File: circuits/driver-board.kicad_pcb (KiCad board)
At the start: 4 copper layers, 40 x 47 mm, 72 parts, among them J1 Conn_01x18_Female, J2 USB4120-03-C_REVA, J3 Motor_Conn_01x04, J4 Screw_Terminals, J5 Conn_01x06_Female, Q1 SS8050-G, Q2 SS8050-G, SW1 RST_SW_Push, U1 CP2102N-A01-GQFN24, U2 BA33DD0T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

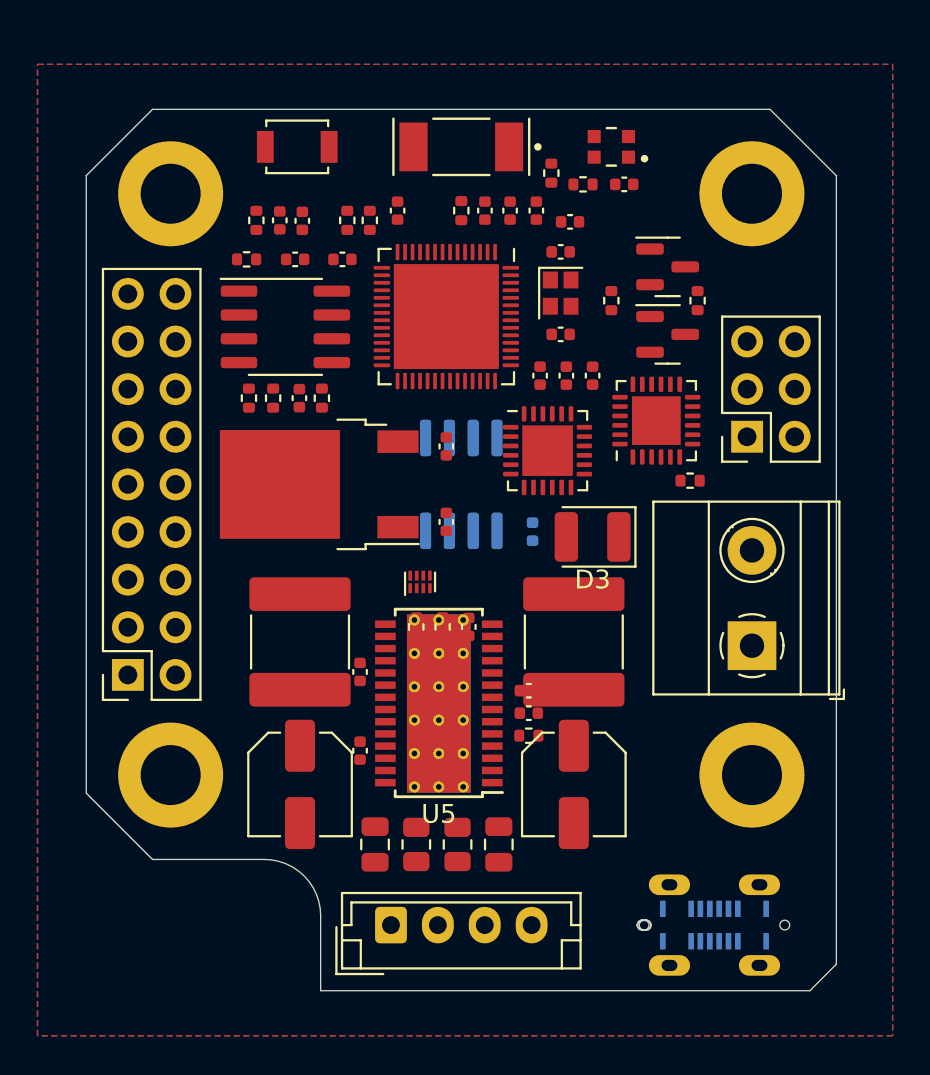
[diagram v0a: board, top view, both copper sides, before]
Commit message: pcb layout redone
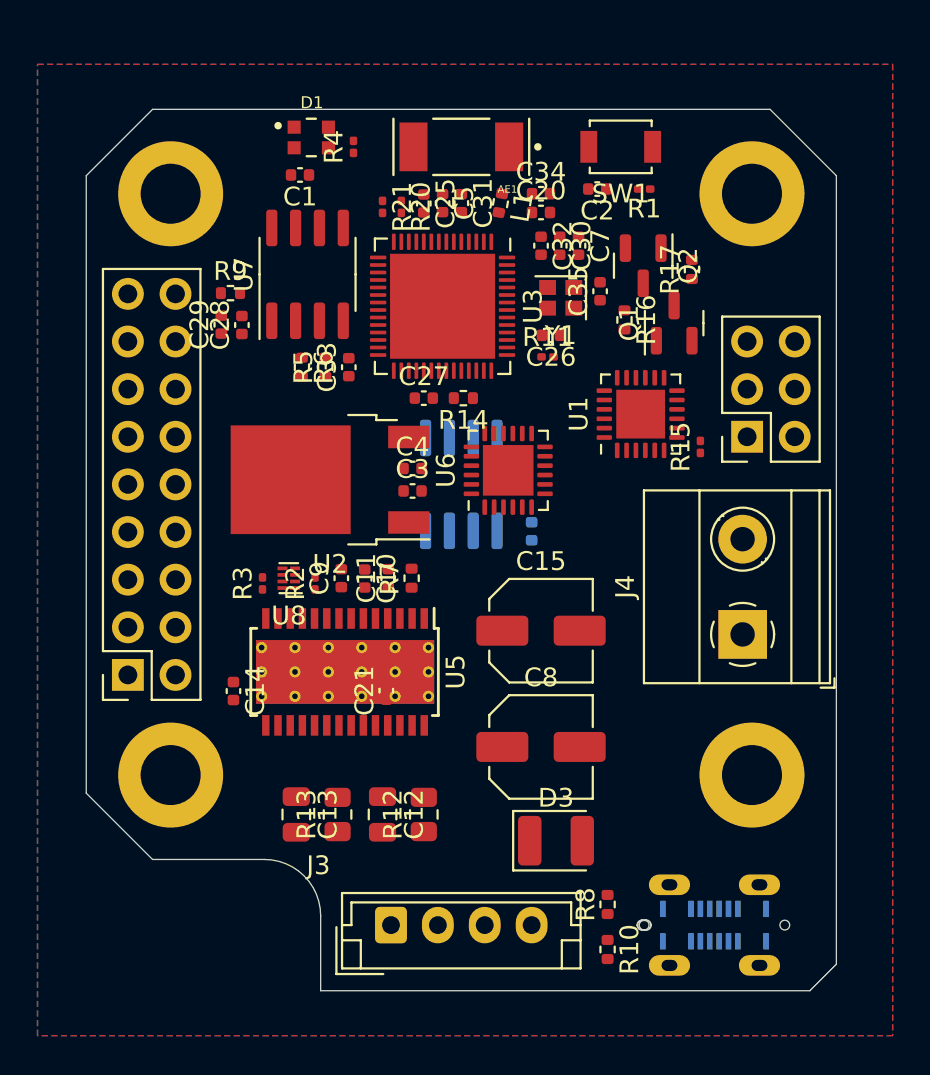
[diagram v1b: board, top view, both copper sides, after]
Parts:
- removed C18: 100nF, Capacitor_SMD:C_0402_1005Metric
- removed C19: 330µF-50V, Capacitor_SMD:C_Elec_5x5.4
- removed C22, C23: 10µF-50V, Capacitor_SMD:C_2220_5650Metric
- added C14: 100nF, Capacitor_SMD:C_0402_1005Metric, F.Cu at (37.9, 61.0)
- added C15: 300µF-50V, Capacitor_SMD:C_Elec_5x5.4, F.Cu at (54.2, 57.8)
- added R20: 4K7, Resistor_SMD:R_0201_0603Metric, F.Cu at (46.8, 35.2)
- added R21: 4K7, Resistor_SMD:R_0201_0603Metric, F.Cu at (45.8, 35.2)
- C8: value 330µF-50V -> 300µF-50V
- R1, R11, R15, R2, R3, R4: footprint Resistor_SMD:R_0402_1005Metric -> Resistor_SMD:R_0201_0603Metric
- R10, R8: value 4K7 -> 5K1
- U1: value CP2102N-A01-GQFN24 -> CP2102N-Axx-xQFN24
- moved R10 40.9 mm to (57.8, 74.8), turned to -90 degrees
- moved R8 39.0 mm to (57.8, 72.4)
- moved R3 22.5 mm to (39.4, 55.3)
- moved R1 20.7 mm to (59.8, 34.2), turned to 180 degrees
- moved C1 17.3 mm to (41.4, 33.5)
- moved SW1 17.2 mm to (58.5, 32.0), turned to 180 degrees
- moved C2 17.0 mm to (57.2, 34.2), turned to 180 degrees
- moved D3 16.3 mm to (55.0, 69.0), turned to 0 degrees
- moved R11 16.0 mm to (54.6, 43.2), turned to 0 degrees
- moved D1 16.0 mm to (42.0, 31.5), turned to 0 degrees
- moved C8 13.0 mm to (54.2, 64.0), turned to 0 degrees
- moved R4 12.4 mm to (44.2, 32.0), turned to 90 degrees
- moved C10 10.6 mm to (44.9, 55.0), turned to -90 degrees
- moved R7 10.5 mm to (47.4, 55.0), turned to 90 degrees
- moved C11 10.4 mm to (46.1, 55.0), turned to 90 degrees
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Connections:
- net AS5601_ABI_A renamed /AS5601_A_ITR / ESP_IO11
- net AS5601_ABI_B renamed /AS5601_B_ITR / ESP_IO12
- net CP2102_RTS renamed /CP2102_RTS
- net ESP_EN renamed /ESP_EN
- net ESP_IO00 renamed /ESP_IO00
- net ESP_IO01 renamed /LED / ESP_IO01
- net ESP_IO02 renamed /ESP_IO02
- net ESP_IO03 renamed /ESP_IO03
- net ESP_IO06 renamed /TMC2209_EN / ESP_IO06
- net ESP_IO07 renamed /TMC2209_STEP / ESP_IO07
- net ESP_IO08 renamed /TMC2209_DIR / ESP_IO08
- net ESP_IO13 renamed /ESP_IO13
- net ESP_IO14 renamed /ESP_IO14
- net ESP_IO17 renamed /ESP_IO17
- net ESP_IO18 renamed /ESP_IO18
- net ESP_IO21 renamed /ESP_IO21
- net ESP_IO43 renamed /UART0_TXD / ESP_IO43
- net ESP_IO45 renamed /UART1_TXD / ESP_IO45
- net ESP_IO46 renamed /UART1_RXD / ESP_IO46
- net ESP_SPICLK renamed /SPICLK / ESP_IO30
- net ESP_SPICS1 renamed /SPICS1 / ESP_IO26
- net ESP_SPID renamed /SPID / ESP_IO32
- net ESP_SPIHD renamed /SPIHD / ESP_IO27
- net ESP_SPIQ renamed /SPIQ / ESP_IO31
- net ESP_SPIVDD renamed /ESP_SPIVDD
- net ESP_SPIWP renamed /SPIWP / ESP_IO28
- net ESP_XTAL_N renamed /XTAL_N
- net ESP_XTAL_P renamed /XTAL_P
- net Net-(C27-Pad2) renamed /ESP_IO47
- net TMC2209_DIAG renamed /TMC2209_DIAG
- J1 pad 15: ESP_IO05 -> /I2C_SDA / ESP_IO05
- J1 pad 16: ESP_IO04 -> /I2C_SCL / ESP_IO04
- J1 pad 9: ESP_IO19 -> /USB_D- / ESP_IO19
- J2 pad A5: USB_CC1 -> /USB_CC1
- J2 pad A6: USB_D+ -> /USB_D+
- J2 pad A7: USB_D- -> /USB_D-
- J2 pad B5: USB_CC2 -> /USB_CC2
- J2 pad B6: USB_D+ -> /USB_D+
- J2 pad B7: USB_D- -> /USB_D-
- J3 pad 1: TMC2209_OB2 -> Net-(J3-Pad1)
- J3 pad 2: TMC2209_OB1 -> Net-(J3-Pad2)
- J3 pad 3: TMC2209_OA1 -> Net-(J3-Pad3)
- J3 pad 4: TMC2209_OA2 -> Net-(J3-Pad4)
- J5 pad 5: ESP_IO44 -> /UART0_RXD / ESP_IO44
- Q2 pad 2: CP2102_DTR -> /CP2102_DTR
- R10 pad 1: +3V3 -> /USB_CC2
- R10 pad 2: ESP_IO04 -> GND
- R16 pad 1: CP2102_DTR -> /CP2102_DTR
- R3 pad 2: ESP_IO10 -> /SR_S / ESP_IO10
- R8 pad 1: +3V3 -> /USB_CC1
- R8 pad 2: ESP_IO05 -> GND
- U1 pad 20: ESP_IO44 -> /UART0_RXD / ESP_IO44
- U1 pad 22: unconnected-(U1-Pad22) -> /CP2102_DTR
- U1 pad 23: CP2102_DTR -> unconnected-(U1-Pad23)
- U1 pad 3: USB_D+ -> /USB_D+
- U1 pad 4: USB_D- -> /USB_D-
- U3 pad 10: ESP_IO05 -> /I2C_SDA / ESP_IO05
- U3 pad 14: ESP_IO09 -> /ESP_IO09
- U3 pad 15: ESP_IO10 -> /ESP_IO10
- U3 pad 25: USB_D- -> /USB_D- / ESP_IO19
- U3 pad 26: USB_D+ -> /USB_D+ / ESP_IO20
- U3 pad 50: unconnected-(U3-Pad50) -> /UART0_RXD / ESP_IO44
- U3 pad 9: ESP_IO04 -> /I2C_SCL / ESP_IO04
- U4 pad 6: ESP_IO05 -> /I2C_SDA / ESP_IO05
- U4 pad 7: ESP_IO04 -> /I2C_SCL / ESP_IO04
- U5 pad 1: TMC2209_OB2 -> Net-(J3-Pad4)
- U5 pad 21: TMC2209_OA2 -> Net-(J3-Pad1)
- U5 pad 24: TMC2209_OA1 -> Net-(J3-Pad2)
- U5 pad 26: TMC2209_OB1 -> Net-(J3-Pad3)
- U6 pad 1: USB_CC1 -> /USB_CC1
- U6 pad 2: USB_CC1 -> /USB_CC1
- U6 pad 4: USB_CC2 -> /USB_CC2
- U6 pad 5: USB_CC2 -> /USB_CC2
- U6 pad 7: ESP_IO04 -> /I2C_SCL / ESP_IO04
- U6 pad 8: ESP_IO05 -> /I2C_SDA / ESP_IO05
- U8 pad 5: ESP_IO09 -> /SR_Q / ESP_IO09
- U8 pad 6: ESP_IO10 -> /SR_S / ESP_IO10
- U8 pad 7: ESP_IO09 -> /SR_Q / ESP_IO09
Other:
- rule pad_to_mask_clearance: 0.051 -> 0

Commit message: adjusted tmc2209 circuitry and redid overall comp placement
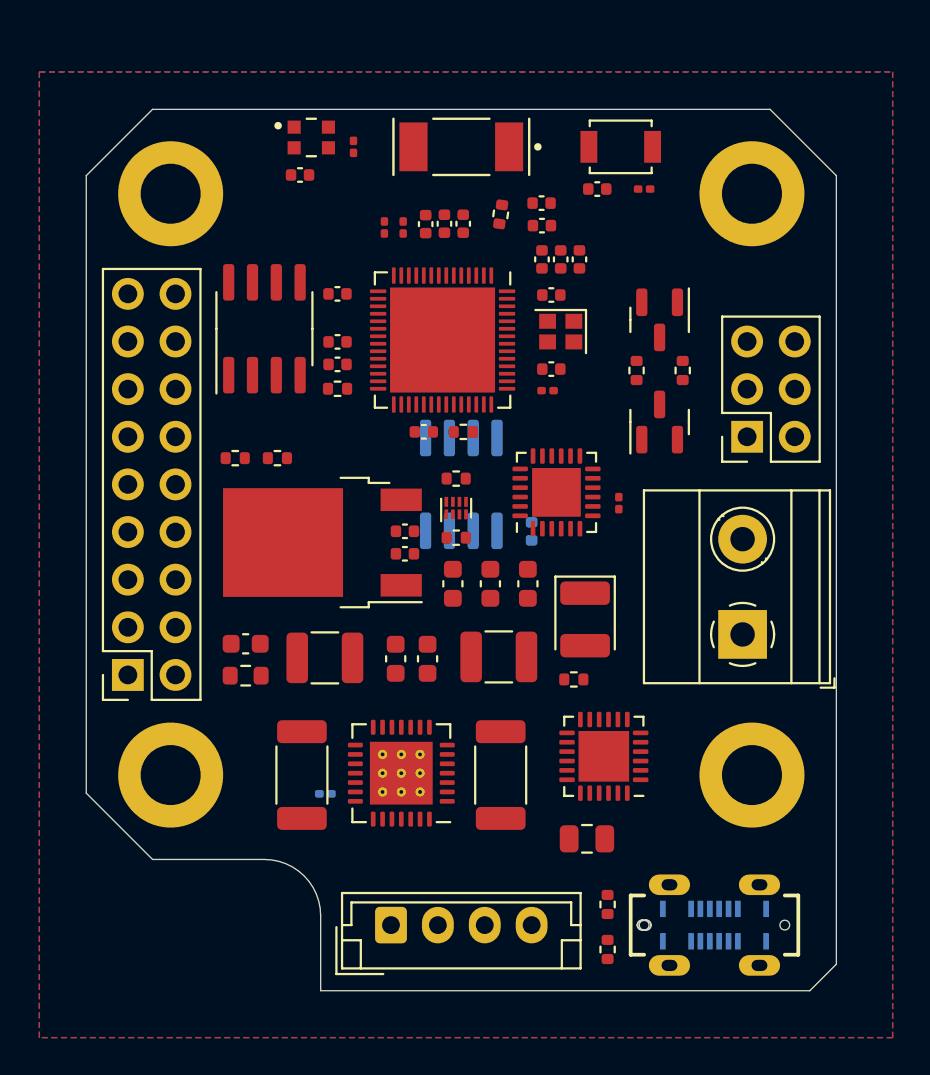
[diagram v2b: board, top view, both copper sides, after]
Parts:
- removed C21: 100nF-50V, Capacitor_SMD:C_0402_1005Metric
- added C16: 10µF-50V, Capacitor_SMD:C_1210_3225Metric, F.Cu at (52.0, 59.2)
- added R18: 20K, Resistor_SMD:R_0402_1005Metric, F.Cu at (49.7, 49.7)
- added R19: 100K, Resistor_SMD:R_0201_0603Metric, B.Cu at (42.8, 66.5)
- C10, C14, C9: footprint Capacitor_SMD:C_0402_1005Metric -> Capacitor_SMD:C_0603_1608Metric
- C11: value 22nF-50V-0603 -> 22nF-50V; footprint Capacitor_SMD:C_0402_1005Metric -> Capacitor_SMD:C_0805_2012Metric
- C12, C13: value 100nF -> 100nF-50V; footprint Capacitor_SMD:C_0805_2012Metric -> Capacitor_SMD:C_0603_1608Metric
- C15: value 300µF-50V -> 10µF-50V; footprint Capacitor_SMD:C_Elec_5x5.4 -> Capacitor_SMD:C_1210_3225Metric
- C8: value 300µF-50V -> 1µF-50V; footprint Capacitor_SMD:C_Elec_5x5.4 -> Capacitor_SMD:C_0603_1608Metric
- R12, R13: value 0R11-0805-1W -> 0R100; footprint Resistor_SMD:R_0805_2012Metric -> Resistor_SMD:R_2010_5025Metric
- R2: footprint Resistor_SMD:R_0201_0603Metric -> Resistor_SMD:R_0402_1005Metric
- R3: value 20K -> 0R100-0603; footprint Resistor_SMD:R_0201_0603Metric -> Resistor_SMD:R_0603_1608Metric
- U5: footprint Package_SO:HTSSOP-28-1EP_4.4x9.7mm_P0.65mm_EP3.4x9.5mm_ThermalVias -> Package_DFN_QFN:QFN-28-1EP_5x5mm_P0.5mm_EP3.35x3.35mm_ThermalVias
- moved C11 17.5 mm to (56.7, 68.9), turned to 180 degrees
- moved C14 16.7 mm to (53.5, 55.3), turned to 90 degrees
- moved C8 16.7 mm to (38.5, 58.5)
- moved U6 16.1 mm to (57.6, 64.5), turned to 180 degrees
- moved D3 11.9 mm to (56.6, 57.2), turned to -90 degrees
- moved C15 11.6 mm to (42.7, 59.2)
- moved C13 10.9 mm to (48.2, 59.3), turned to 90 degrees
- moved R7 10.2 mm to (56.0, 60.4), turned to 0 degrees
- moved U8 9.68 mm to (49.7, 51.3), turned to 90 degrees
- moved R13 8.95 mm to (52.1, 65.5), turned to -90 degrees
- moved C12 8.33 mm to (46.5, 59.3), turned to 90 degrees
- moved R2 7.91 mm to (49.7, 52.8), turned to 0 degrees
- moved R9 7.66 mm to (43.4, 44.9), turned to 180 degrees
- moved R12 6.83 mm to (41.5, 65.5), turned to -90 degrees
- moved C10 6.71 mm to (51.5, 55.3)
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- renumbered U7 to U
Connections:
- net /XTAL_N renamed Net-(U3-Pad53)
- net /XTAL_P renamed Net-(C35-Pad2)
- net Net-(J3-Pad1) renamed /TMC2209_OA2
- net Net-(J3-Pad2) renamed /TMC2209_OA1
- net Net-(J3-Pad3) renamed /TMC2209_OB1
- net Net-(J3-Pad4) renamed /TMC2209_OB2
- C12 pad 1: Net-(C12-Pad1) -> VBUS
- C13 pad 1: Net-(C13-Pad1) -> VBUS
- C8 pad 2: GND -> Net-(C8-Pad2)
- R12 pad 2: Net-(C12-Pad1) -> Net-(R12-Pad2)
- R13 pad 2: Net-(C13-Pad1) -> Net-(R13-Pad2)
- R2 pad 1: /TMC2209_DIAG -> +3V3
- R2 pad 2: GND -> /SR_S / ESP_IO10
- R3 pad 1: +3V3 -> Net-(C8-Pad2)
- R3 pad 2: /SR_S / ESP_IO10 -> GND
- U5 pad 20: GND -> Net-(U5-Pad20)
- U5 pad 23: Net-(C12-Pad1) -> Net-(R12-Pad2)
- U5 pad 27: Net-(C13-Pad1) -> Net-(R13-Pad2)
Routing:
- added copper zone on In2.Cu, net +3V3
- added copper zone on In2.Cu, net VBUS

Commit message: labels on pcb
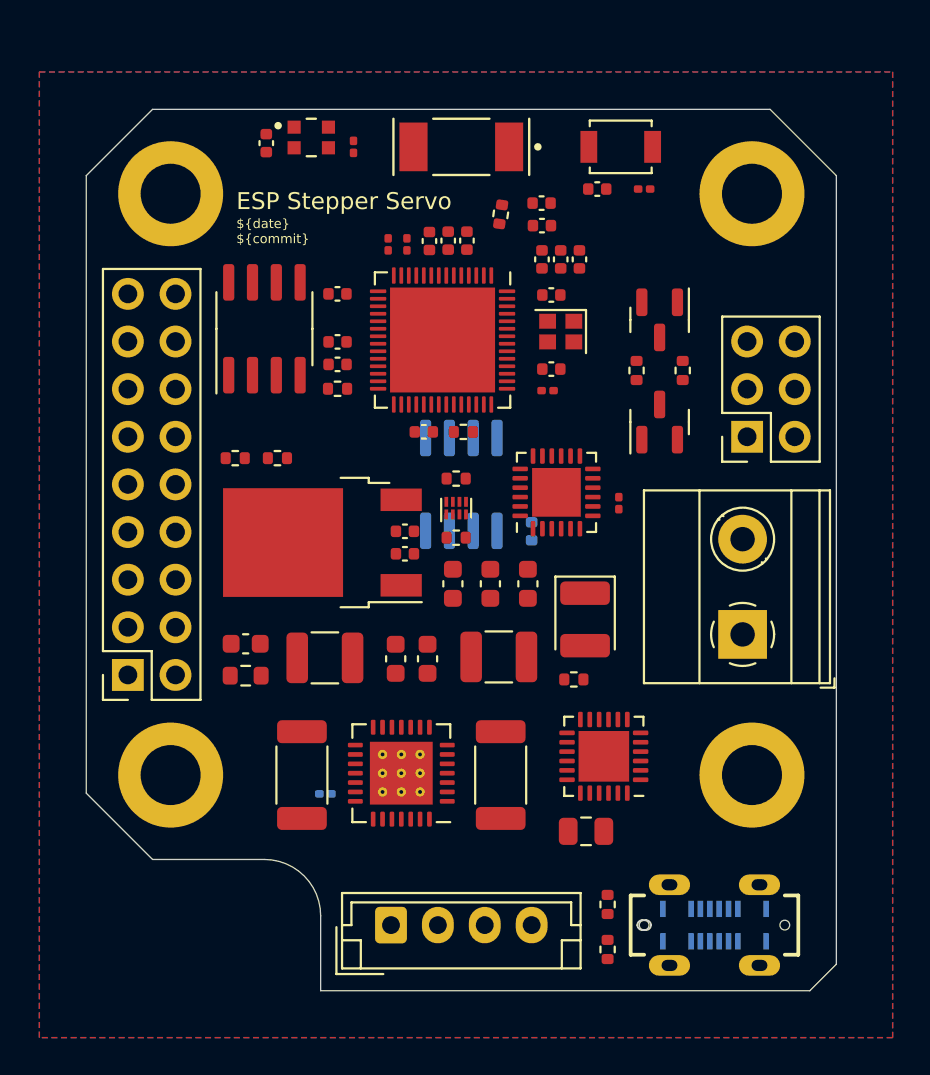
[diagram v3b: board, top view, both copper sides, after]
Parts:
- moved C1 2.48 mm to (39.6, 31.8), turned to -90 degrees
- moved R20 0.92 mm to (47.1, 37.2)
- moved R21 0.92 mm to (46.1, 37.2)
- moved C25 0.92 mm to (48.3, 37.0)
- moved C31 0.92 mm to (50.3, 37.0)
- moved C5 0.92 mm to (49.3, 37.0)
- moved C11 0.40 mm to (56.6, 68.5)
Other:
- board text added: "${date}"
- board text added: "${date} ${commit}"
- board text added: "ESP Stepper Servo"
- board text added: "by Christian Skjerning"
- board text added: "github.com/slimcdk/esp-stepper-servo @ ${commit}"
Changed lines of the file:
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@@
   )
   (footprint "Resistor_SMD:R_0201_0603Metric" (layer "F.Cu")
-    (at 46.9 36.3 -90)
+    (at 47.1 37.2 -90)
     (descr "Resistor SMD 0201 (0603 Metric), square (rectangular) end terminal, IPC_7351 nominal, (Body size source: https://www.vishay.com/docs/20052/crcw0201e3.pdf), generated with kicad-footprint-generator")
     (tags "resistor")
@@
   )
   (footprint "Capacitor_SMD:C_0402_1005Metric" (layer "F.Cu")
-    (at 41.4 33.5 180)
+    (at 39.6 31.8 -90)
     (descr "Capacitor SMD 0402 (1005 Metric), square (rectangular) end terminal, IPC_7351 nominal, (Body size source: IPC-SM-782 page 76, https://www.pcb-3d.com/wordpress/wp-content/uploads/ipc-sm-782a_amendment_1_and_2.pdf), generated with kicad-footprint-generator")
     (tags "capacitor")
@@
     (property "Sheetname" "")
     (attr smd)
-    (fp_text reference "C1" (at 0 -1.16) (layer "F.SilkS") hide
+    (fp_text reference "C1" (at 0 -1.16 -270) (layer "F.SilkS") hide
       (effects (font (size 1 1) (thickness 0.15)))
     )
-    (fp_text value "100nF" (at 0 1.16) (layer "F.Fab")
+    (fp_text value "100nF" (at 0 1.16 -270) (layer "F.Fab")
       (effects (font (size 1 1) (thickness 0.15)))
     )
-    (fp_text user "${REFERENCE}" (at 0 0) (layer "F.Fab")
+    (fp_text user "${REFERENCE}" (at 0 0 -270) (layer "F.Fab")
       (effects (font (size 0.25 0.25) (thickness 0.04)))
     )
@@
     (fp_line (start -0.5 -0.25) (end 0.5 -0.25) (layer "F.Fab") (width 0.1))
     (fp_line (start -0.5 0.25) (end -0.5 -0.25) (layer "F.Fab") (width 0.1))
-    (pad "1" smd roundrect (at -0.48 0 180) (size 0.56 0.62) (layers "F.Cu" "F.Paste" "F.Mask") (roundrect_rratio 0.25)
+    (pad "1" smd roundrect (at -0.48 0 270) (size 0.56 0.62) (layers "F.Cu" "F.Paste" "F.Mask") (roundrect_rratio 0.25)
       (net 2 "+3V3") (pintype "passive"))
-    (pad "2" smd roundrect (at 0.48 0 180) (size 0.56 0.62) (layers "F.Cu" "F.Paste" "F.Mask") (roundrect_rratio 0.25)
+    (pad "2" smd roundrect (at 0.48 0 270) (size 0.56 0.62) (layers "F.Cu" "F.Paste" "F.Mask") (roundrect_rratio 0.25)
       (net 1 "GND") (pintype "passive"))
     (model "${KICAD6_3DMODEL_DIR}/Capacitor_SMD.3dshapes/C_0402_1005Metric.wrl"
@@
   )
   (footprint "Capacitor_SMD:C_0402_1005Metric" (layer "F.Cu")
-    (at 49.1 36.1 -90)
+    (at 49.3 37 -90)
     (descr "Capacitor SMD 0402 (1005 Metric), square (rectangular) end terminal, IPC_7351 nominal, (Body size source: IPC-SM-782 page 76, https://www.pcb-3d.com/wordpress/wp-content/uploads/ipc-sm-782a_amendment_1_and_2.pdf), generated with kicad-footprint-generator")
     (tags "capacitor")
@@
   )
   (footprint "Resistor_SMD:R_0201_0603Metric" (layer "F.Cu")
-    (at 45.9 36.3 -90)
+    (at 46.1 37.2 -90)
     (descr "Resistor SMD 0201 (0603 Metric), square (rectangular) end terminal, IPC_7351 nominal, (Body size source: https://www.vishay.com/docs/20052/crcw0201e3.pdf), generated with kicad-footprint-generator")
     (tags "resistor")
@@
   )
   (footprint "Capacitor_SMD:C_0402_1005Metric" (layer "F.Cu")
-    (at 50.1 36.1 -90)
+    (at 50.3 37 -90)
     (descr "Capacitor SMD 0402 (1005 Metric), square (rectangular) end terminal, IPC_7351 nominal, (Body size source: IPC-SM-782 page 76, https://www.pcb-3d.com/wordpress/wp-content/uploads/ipc-sm-782a_amendment_1_and_2.pdf), generated with kicad-footprint-generator")
     (tags "capacitor")
@@
   )
   (footprint "Capacitor_SMD:C_0805_2012Metric" (layer "F.Cu")
-    (at 56.7 68.9 180)
+    (at 56.65 68.5 180)
     (descr "Capacitor SMD 0805 (2012 Metric), square (rectangular) end terminal, IPC_7351 nominal, (Body size source: IPC-SM-782 page 76, https://www.pcb-3d.com/wordpress/wp-content/uploads/ipc-sm-782a_amendment_1_and_2.pdf, https://docs.google.com/spreadsheets/d/1BsfQQcO9C6DZCsRaXUlFlo91Tg2WpOkGARC1WS5S8t0/edit?usp=sharing), generated with kicad-footprint-generator")
     (tags "capacitor")
@@
   )
   (footprint "Capacitor_SMD:C_0402_1005Metric" (layer "F.Cu")
-    (at 48.1 36.12 -90)
+    (at 48.3 37.02 -90)
     (descr "Capacitor SMD 0402 (1005 Metric), square (rectangular) end terminal, IPC_7351 nominal, (Body size source: IPC-SM-782 page 76, https://www.pcb-3d.com/wordpress/wp-content/uploads/ipc-sm-782a_amendment_1_and_2.pdf), generated with kicad-footprint-generator")
     (tags "capacitor")
@@
   (gr_line locked (start 68.586 77) (end 70 75.586) (layer "Edge.Cuts") (width 0.05))
   (gr_line locked (start 30 66.464) (end 33.536 70) (layer "Edge.Cuts") (width 0.05))
+  (gr_text "${date}" (at 54.3 39.7 270) (layer "B.SilkS")
+    (effects (font (size 1 1) (thickness 0.2)) (justify mirror))
+  )
+  (gr_text "github.com/slimcdk/esp-stepper-servo\n@ ${commit}" (at 55.105 65.32381 270) (layer "B.SilkS")
+    (effects (font (size 1 1) (thickness 0.2)) (justify left mirror))
+  )
+  (gr_text "ESP Stepper Servo" (at 59.95 70.126191 270) (layer "B.SilkS")
+    (effects (font (size 1.5 1.5) (thickness 0.3)) (justify left mirror))
+  )
+  (gr_text "by Christian Skjerning" (at 57.8 65.57381 270) (layer "B.SilkS")
+    (effects (font (size 1 1) (thickness 0.2)) (justify left mirror))
+  )
+  (gr_text "ESP Stepper Servo" (at 38 34.9) (layer "F.SilkS")
+    (effects (font (size 0.9 0.9) (thickness 0.15)) (justify left))
+  )
+  (gr_text "${date}\n${commit}" (at 38 36.5) (layer "F.SilkS")
+    (effects (font (size 0.5 0.5) (thickness 0.1)) (justify left))
+  )
   (segment (start 46.425 73.325) (end 46.25 73.5) (width 0.25) (layer "F.Cu") (net 35))
   (zone (net 1) (net_name "GND") (layer "F.Cu") (hatch edge 0.508)
@@
     )
   )
+  (group "" (id 0eae2e0e-e2ed-4ce6-8b96-8c794733a464)
+    (members
+      02202713-7675-4f1c-96a1-11a55b38985c
+      a8c34281-5d19-49a6-af10-73ddc741e8ed
+    )
+  )
+  (group "" (id 19fd82a3-5ed3-41f6-aacc-044bbfc3f9df)
+    (members
+      c0b18ac4-b82f-4beb-b300-6d260a3a722c
+      dd63db8b-4398-48ec-a42a-62c0518c461d
+    )
+  )
   (group "" (id 37c7449d-97f5-43f2-bbfc-d314bfd0349a)
     (members
@@
     )
   )
+  (group "" (id 9e660ba1-5792-4812-9fdf-4dc5cba90caf)
+    (members
+      0eae2e0e-e2ed-4ce6-8b96-8c794733a464
+      d977e0ef-5ce5-45e5-a918-4e3afd534a91
+      fb2c7631-881e-463a-a556-d17783d4340b
+    )
+  )
